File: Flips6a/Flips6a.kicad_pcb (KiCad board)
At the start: 2 copper layers, 90 x 50 mm, 28 parts, among them CN201 Conn_02x05_Odd_Even, CN301 Conn_02x05_Odd_Even, CN401 Conn_02x05_Odd_Even, CN501 Conn_02x05_Odd_Even, CN601 Conn_02x05_Odd_Even, CN701 Conn_02x05_Odd_Even, CN801 Conn_02x05_Odd_Even, J101 Conn_02x04_Odd_Even, U201 74HCT595, U301 74HCT595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

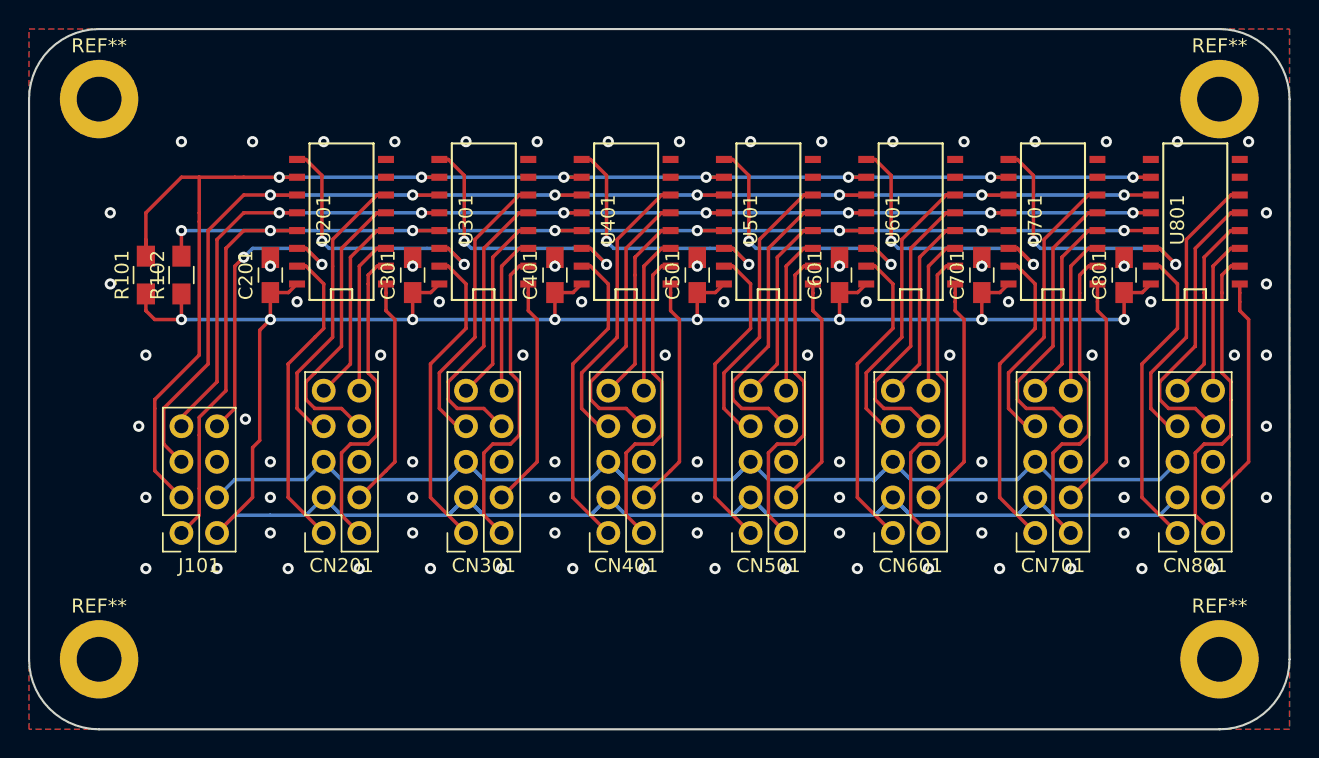
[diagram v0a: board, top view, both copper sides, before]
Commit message: switch flips 6a to use own UFP2810 connector
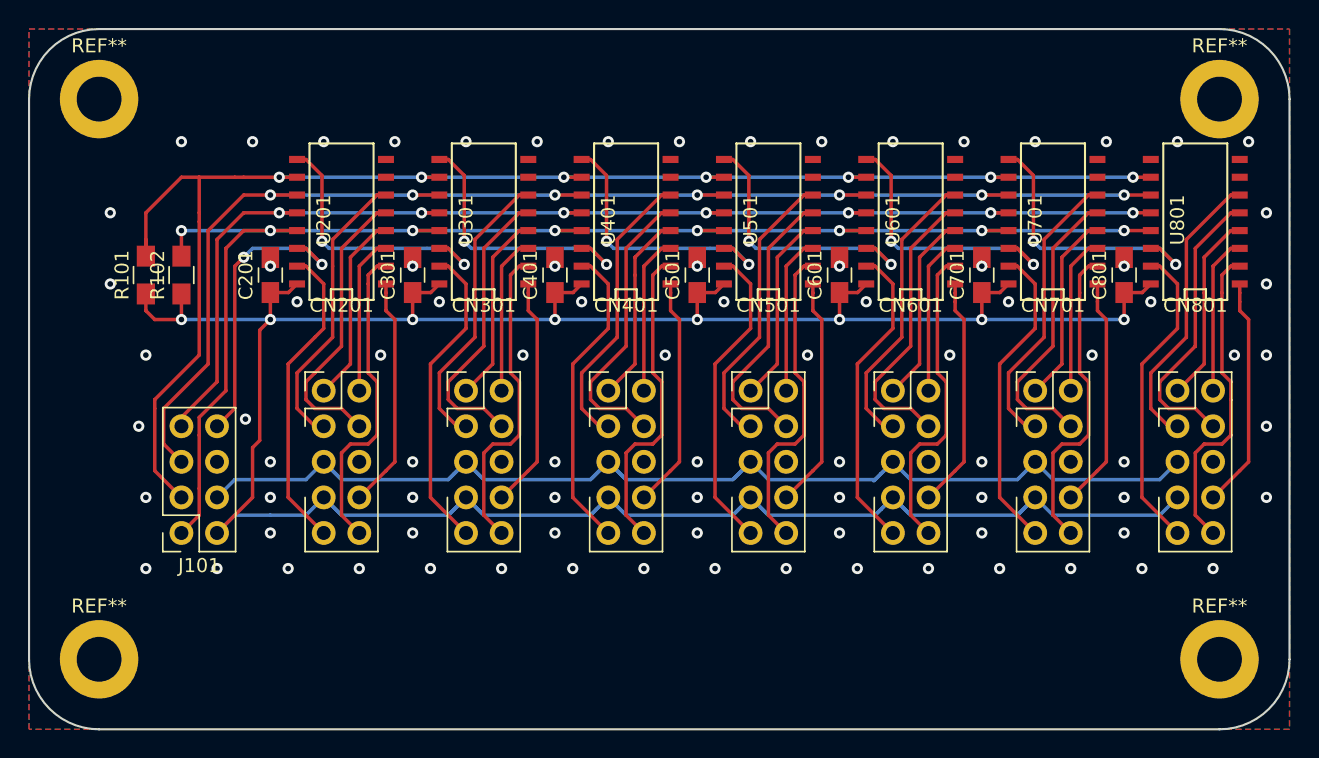
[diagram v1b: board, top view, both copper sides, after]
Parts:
- CN201, CN301, CN401, CN501, CN601, CN701, CN801: value Conn_02x05_Odd_Even -> UFP2810; footprint Socket_Strips:Socket_Strip_Straight_2x05_Pitch2.54mm -> Own:Pin_Header_Straight_Shrouded_2x05_Pitch2.54mm
- moved CN201 10.2 mm to (193.0, 83.8), turned to 0 degrees
- moved CN301 10.2 mm to (203.2, 83.8), turned to 0 degrees
- moved CN401 10.2 mm to (213.4, 83.8), turned to 0 degrees
- moved CN501 10.2 mm to (223.5, 83.8), turned to 0 degrees
- moved CN601 10.2 mm to (233.7, 83.8), turned to 0 degrees
- moved CN701 10.2 mm to (243.8, 83.8), turned to 0 degrees
- moved CN801 10.2 mm to (254.0, 83.8), turned to 0 degrees
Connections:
- CN201 pad 1: /ShiftRegister2/A0 -> /ShiftRegister2/B1
- CN201 pad 10: /ShiftRegister2/B0 -> /ShiftRegister2/A2
- CN201 pad 2: /ShiftRegister2/A2 -> /ShiftRegister2/B0
- CN201 pad 3: +5V -> /ShiftRegister2/EN
- CN201 pad 4: /ShiftRegister2/A1 -> /ShiftRegister2/DATA
- CN201 pad 7: /ShiftRegister2/EN -> +5V
- CN201 pad 8: /ShiftRegister2/DATA -> /ShiftRegister2/A1
- CN201 pad 9: /ShiftRegister2/B1 -> /ShiftRegister2/A0
- CN301 pad 1: /ShiftRegister3/A0 -> /ShiftRegister3/B1
- CN301 pad 10: /ShiftRegister3/B0 -> /ShiftRegister3/A2
- CN301 pad 2: /ShiftRegister3/A2 -> /ShiftRegister3/B0
- CN301 pad 3: +5V -> /ShiftRegister3/EN
- CN301 pad 4: /ShiftRegister3/A1 -> /ShiftRegister3/DATA
- CN301 pad 7: /ShiftRegister3/EN -> +5V
- CN301 pad 8: /ShiftRegister3/DATA -> /ShiftRegister3/A1
- CN301 pad 9: /ShiftRegister3/B1 -> /ShiftRegister3/A0
- CN401 pad 1: /ShiftRegister4/A0 -> /ShiftRegister4/B1
- CN401 pad 10: /ShiftRegister4/B0 -> /ShiftRegister4/A2
- CN401 pad 2: /ShiftRegister4/A2 -> /ShiftRegister4/B0
- CN401 pad 3: +5V -> /ShiftRegister4/EN
- CN401 pad 4: /ShiftRegister4/A1 -> /ShiftRegister4/DATA
- CN401 pad 7: /ShiftRegister4/EN -> +5V
- CN401 pad 8: /ShiftRegister4/DATA -> /ShiftRegister4/A1
- CN401 pad 9: /ShiftRegister4/B1 -> /ShiftRegister4/A0
- CN501 pad 1: /ShiftRegister5/A0 -> /ShiftRegister5/B1
- CN501 pad 10: /ShiftRegister5/B0 -> /ShiftRegister5/A2
- CN501 pad 2: /ShiftRegister5/A2 -> /ShiftRegister5/B0
- CN501 pad 3: +5V -> /ShiftRegister5/EN
- CN501 pad 4: /ShiftRegister5/A1 -> /ShiftRegister5/DATA
- CN501 pad 7: /ShiftRegister5/EN -> +5V
- CN501 pad 8: /ShiftRegister5/DATA -> /ShiftRegister5/A1
- CN501 pad 9: /ShiftRegister5/B1 -> /ShiftRegister5/A0
- CN601 pad 1: /ShiftRegister6/A0 -> /ShiftRegister6/B1
- CN601 pad 10: /ShiftRegister6/B0 -> /ShiftRegister6/A2
- CN601 pad 2: /ShiftRegister6/A2 -> /ShiftRegister6/B0
- CN601 pad 3: +5V -> /ShiftRegister6/EN
- CN601 pad 4: /ShiftRegister6/A1 -> /ShiftRegister6/DATA
- CN601 pad 7: /ShiftRegister6/EN -> +5V
- CN601 pad 8: /ShiftRegister6/DATA -> /ShiftRegister6/A1
- CN601 pad 9: /ShiftRegister6/B1 -> /ShiftRegister6/A0
- CN701 pad 1: /ShiftRegister7/A0 -> /ShiftRegister7/B1
- CN701 pad 10: /ShiftRegister7/B0 -> /ShiftRegister7/A2
- CN701 pad 2: /ShiftRegister7/A2 -> /ShiftRegister7/B0
- CN701 pad 3: +5V -> /ShiftRegister7/EN
- CN701 pad 4: /ShiftRegister7/A1 -> /ShiftRegister7/DATA
- CN701 pad 7: /ShiftRegister7/EN -> +5V
- CN701 pad 8: /ShiftRegister7/DATA -> /ShiftRegister7/A1
- CN701 pad 9: /ShiftRegister7/B1 -> /ShiftRegister7/A0
- CN801 pad 1: /ShiftRegister8/A0 -> /ShiftRegister8/B1
- CN801 pad 10: /ShiftRegister8/B0 -> /ShiftRegister8/A2
- CN801 pad 2: /ShiftRegister8/A2 -> /ShiftRegister8/B0
- CN801 pad 3: +5V -> /ShiftRegister8/EN
- CN801 pad 4: /ShiftRegister8/A1 -> /ShiftRegister8/DATA
- CN801 pad 7: /ShiftRegister8/EN -> +5V
- CN801 pad 8: /ShiftRegister8/DATA -> /ShiftRegister8/A1
- CN801 pad 9: /ShiftRegister8/B1 -> /ShiftRegister8/A0
- U201 pad 7: (no net) -> Net-(U201-Pad7)
- U301 pad 7: (no net) -> Net-(U301-Pad7)
- U401 pad 7: (no net) -> Net-(U401-Pad7)
- U501 pad 7: (no net) -> Net-(U501-Pad7)
- U601 pad 7: (no net) -> Net-(U601-Pad7)
- U701 pad 7: (no net) -> Net-(U701-Pad7)
- U801 pad 7: (no net) -> Net-(U801-Pad7)
- U801 pad 9: (no net) -> /ShiftRegister8/DOUT
